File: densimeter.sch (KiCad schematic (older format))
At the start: 3 parts, among them IC1 XGZP6897A

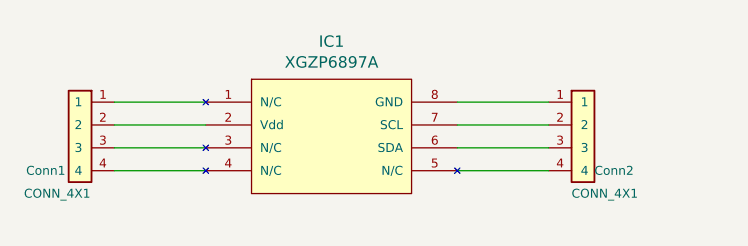
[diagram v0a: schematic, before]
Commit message: added 100 nF capacitor C1
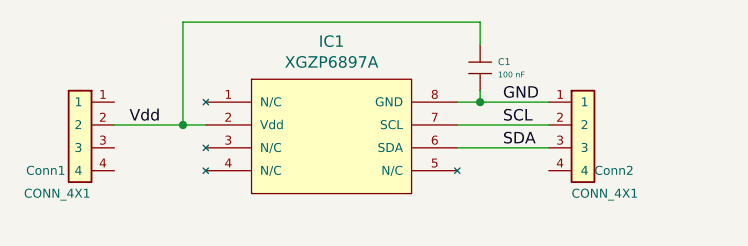
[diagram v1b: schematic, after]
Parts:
- added C1: 100 nF, Capacitor_SMD:C_0805_2012Metric, symbol thmalmeida:C_Micro
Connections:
- net at IC1.1 (N/C): no longer Conn1.1
- net Vdd: now reaches Conn1.2, IC1.2 (Vdd)
- net Vdd: now also C1.1 (A)
- net at IC1.3 (N/C): no longer Conn1.3
- net at IC1.4 (N/C): no longer Conn1.4
- net at IC1.5 (N/C): no longer Conn2.4
- net SDA: now reaches Conn2.3, IC1.6 (SDA)
- net SCL: now reaches Conn2.2, IC1.7 (SCL)
- net GND: now reaches Conn2.1, IC1.8 (GND)
- net GND: now also C1.2 (B)
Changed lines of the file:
@@
 $EndComp
 Wire Wire Line
-	4950 3300 4550 3300
+	4950 3300 4850 3300
 Wire Wire Line
-	4550 3400 4950 3400
-Wire Wire Line
-	4950 3500 4550 3500
-Wire Wire Line
-	4550 3200 4950 3200
-Wire Wire Line
-	6050 3200 6450 3200
+	6050 3200 6150 3200
 Wire Wire Line
 	6450 3300 6050 3300
@@
 	6050 3400 6450 3400
 Wire Wire Line
-	6450 3500 6050 3500
+	6150 3150 6150 3200
+Connection ~ 6150 3200
+Wire Wire Line
+	6150 3200 6450 3200
+Wire Wire Line
+	6150 2950 6150 2850
+Wire Wire Line
+	6150 2850 4850 2850
+Wire Wire Line
+	4850 2850 4850 3300
+Connection ~ 4850 3300
+Wire Wire Line
+	4850 3300 4550 3300
+$Comp
+L thmalmeida:C_Micro C1
+U 1 1 615E0BAC
+P 6150 3050
+F 0 "C1" H 6228 3076 30  0000 L CNN
+F 1 "100 nF" H 6228 3020 25  0000 L CNN
+F 2 "Capacitor_SMD:C_0805_2012Metric" H 6400 2700 60  0001 C CNN
+F 3 "" H 6190 3100 60  0000 C CNN
+F 4 "xx" H 6400 3200 60  0001 C CNN "Rated Voltage [V]"
+F 5 "xx" H 6400 3300 60  0001 C CNN "Tolerance [%]"
+F 6 "xxxx" H 6400 3100 60  0001 C CNN "Part Number"
+F 7 "yyyy" H 6400 3000 60  0001 C CNN "Manufacture"
+F 8 "xxx" H 6400 2900 60  0001 C CNN "Module"
+F 9 "yes" H 6400 2800 60  0001 C CNN "Placed Onboard?"
+	1    6150 3050
+	1    0    0    -1
+$EndComp
+Text Label 6250 3200 0    50   ~ 0
+GND
+Text Label 6250 3300 0    50   ~ 0
+SCL
+Text Label 6250 3400 0    50   ~ 0
+SDA
+Text Label 4750 3300 2    50   ~ 0
+Vdd
 $EndSCHEMATC

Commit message: 4 pins module
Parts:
- removed Conn1: CONN_4X1, Connector_PinHeader_2.54mm:PinHeader_1x04_P2.54mm_Vertical, symbol thmalmeida:CONN_4X1
- renumbered Conn2 to Conn1
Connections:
- net SCL: now also Conn1.1; no longer Conn1.2
- net SDA: now also Conn1.2; no longer Conn1.3
- net Vdd: now also Conn1.3
- net Gnd: now reaches Conn1.4
- net Gnd: now also C1.2 (B), IC1.8 (GND)
- removed net GND: C1.2 (B), Conn1.1, IC1.8 (GND)
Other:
- moved on the sheet: Conn1
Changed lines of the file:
@@
 $Comp
 L thmalmeida:CONN_4X1 Conn1
-U 1 1 615DF409
-P 4400 3350
-F 0 "Conn1" H 4550 3200 39  0000 C CNN
-F 1 "CONN_4X1" H 4500 3100 39  0000 C CNN
-F 2 "Connector_PinHeader_2.54mm:PinHeader_1x04_P2.54mm_Vertical" H 4430 3080 60  0001 C CNN
-F 3 "" H 4400 3600 60  0000 C CNN
-F 4 "xxxx" H 4400 3650 60  0001 C CNN "Part Number"
-F 5 "MM" H 4400 3750 60  0001 C CNN "Manufacturer"
-F 6 "mm" H 4400 3850 60  0001 C CNN "Module"
-F 7 "no" H 4400 3950 60  0001 C CNN "Placed Onboard?"
-	1    4400 3350
-	-1   0    0    -1
-$EndComp
-$Comp
-L thmalmeida:CONN_4X1 Conn2
 U 1 1 615DF971
-P 6600 3350
-F 0 "Conn2" H 6650 3200 39  0000 L CNN
-F 1 "CONN_4X1" H 6550 3100 39  0000 L CNN
-F 2 "Connector_PinHeader_2.54mm:PinHeader_1x04_P2.54mm_Vertical" H 6630 3080 60  0001 C CNN
-F 3 "" H 6600 3600 60  0000 C CNN
-F 4 "xxxx" H 6600 3650 60  0001 C CNN "Part Number"
-F 5 "MM" H 6600 3750 60  0001 C CNN "Manufacturer"
-F 6 "mm" H 6600 3850 60  0001 C CNN "Module"
-F 7 "no" H 6600 3950 60  0001 C CNN "Placed Onboard?"
-	1    6600 3350
+P 6600 3450
+F 0 "Conn1" V 6700 3300 39  0000 L CNN
+F 1 "CONN_4X1" H 6450 3200 39  0000 L CNN
+F 2 "Connector_PinHeader_2.54mm:PinHeader_1x04_P2.54mm_Vertical" H 6630 3180 60  0001 C CNN
+F 3 "" H 6600 3700 60  0000 C CNN
+F 4 "xxxx" H 6600 3750 60  0001 C CNN "Part Number"
+F 5 "MM" H 6600 3850 60  0001 C CNN "Manufacturer"
+F 6 "mm" H 6600 3950 60  0001 C CNN "Module"
+F 7 "no" H 6600 4050 60  0001 C CNN "Placed Onboard?"
+	1    6600 3450
 	1    0    0    -1
 $EndComp
@@
 Connection ~ 6150 3200
 Wire Wire Line
-	6150 3200 6450 3200
-Wire Wire Line
 	6150 2950 6150 2850
 Wire Wire Line
@@
 Wire Wire Line
 	4850 2850 4850 3300
-Connection ~ 4850 3300
-Wire Wire Line
-	4850 3300 4550 3300
 $Comp
 L thmalmeida:C_Micro C1
@@
 	1    0    0    -1
 $EndComp
-Text Label 6250 3200 0    50   ~ 0
-GND
+Text Label 6400 3600 2    50   ~ 0
+Gnd
 Text Label 6250 3300 0    50   ~ 0
 SCL
 Text Label 6250 3400 0    50   ~ 0
 SDA
-Text Label 4750 3300 2    50   ~ 0
+Text Label 6400 3500 2    50   ~ 0
 Vdd
+Wire Wire Line
+	4850 3300 4850 3700
+Wire Wire Line
+	4850 3700 6150 3700
+Wire Wire Line
+	6150 3700 6150 3500
+Wire Wire Line
+	6150 3500 6450 3500
+Connection ~ 4850 3300
+Wire Wire Line
+	6750 3200 6750 3750
+Wire Wire Line
+	6750 3750 6400 3750
+Wire Wire Line
+	6400 3750 6400 3600
+Wire Wire Line
+	6400 3600 6450 3600
+Wire Wire Line
+	6150 3200 6750 3200
 $EndSCHEMATC

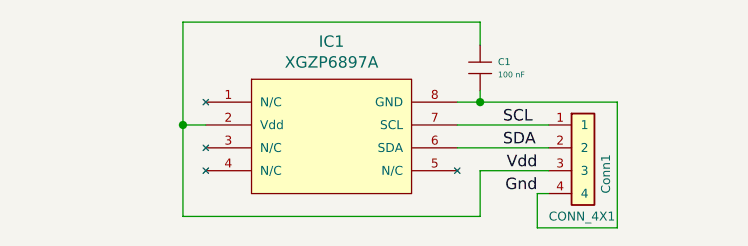
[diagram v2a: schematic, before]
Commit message: pull up resistors added
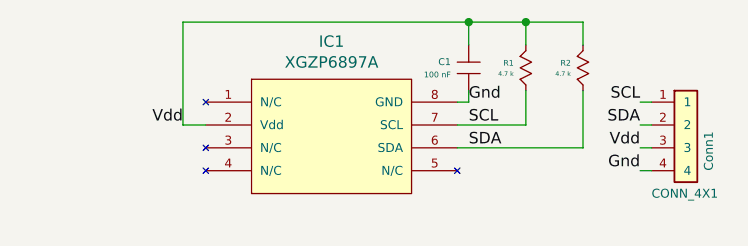
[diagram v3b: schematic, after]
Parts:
- added R1, R2: 4.7 k, Resistor_SMD:R_0805_2012Metric, symbol thmalmeida:R_Micro
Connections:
- net SCL: now also R1.1 (A)
- net SDA: now also R2.1 (A)
- net Vdd: now also R1.2 (B), R2.2 (B)
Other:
- moved on the sheet: C1, Conn1
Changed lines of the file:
@@
 L thmalmeida:CONN_4X1 Conn1
 U 1 1 615DF971
-P 6600 3450
-F 0 "Conn1" V 6700 3300 39  0000 L CNN
-F 1 "CONN_4X1" H 6450 3200 39  0000 L CNN
-F 2 "Connector_PinHeader_2.54mm:PinHeader_1x04_P2.54mm_Vertical" H 6630 3180 60  0001 C CNN
-F 3 "" H 6600 3700 60  0000 C CNN
-F 4 "xxxx" H 6600 3750 60  0001 C CNN "Part Number"
-F 5 "MM" H 6600 3850 60  0001 C CNN "Manufacturer"
-F 6 "mm" H 6600 3950 60  0001 C CNN "Module"
-F 7 "no" H 6600 4050 60  0001 C CNN "Placed Onboard?"
-	1    6600 3450
+P 7050 3350
+F 0 "Conn1" V 7150 3200 39  0000 L CNN
+F 1 "CONN_4X1" H 6900 3100 39  0000 L CNN
+F 2 "Connector_PinHeader_2.54mm:PinHeader_1x04_P2.54mm_Vertical" H 7080 3080 60  0001 C CNN
+F 3 "" H 7050 3600 60  0000 C CNN
+F 4 "xxxx" H 7050 3650 60  0001 C CNN "Part Number"
+F 5 "MM" H 7050 3750 60  0001 C CNN "Manufacturer"
+F 6 "mm" H 7050 3850 60  0001 C CNN "Module"
+F 7 "no" H 7050 3950 60  0001 C CNN "Placed Onboard?"
+	1    7050 3350
 	1    0    0    -1
 $EndComp
@@
 	4950 3300 4850 3300
 Wire Wire Line
-	6050 3200 6150 3200
+	6050 3200 6100 3200
 Wire Wire Line
-	6450 3300 6050 3300
-Wire Wire Line
-	6050 3400 6450 3400
-Wire Wire Line
-	6150 3150 6150 3200
-Connection ~ 6150 3200
-Wire Wire Line
-	6150 2950 6150 2850
-Wire Wire Line
-	6150 2850 4850 2850
+	6100 2850 4850 2850
 Wire Wire Line
 	4850 2850 4850 3300
+Text Label 6850 3200 2    50   ~ 0
+SCL
+Text Label 6850 3300 2    50   ~ 0
+SDA
+$Comp
+L thmalmeida:R_Micro R2
+U 1 1 615EBE8B
+P 6600 3050
+F 0 "R2" H 6547 3029 25  0000 R CNN
+F 1 "4.7 k" H 6547 3076 20  0000 R CNN
+F 2 "Resistor_SMD:R_0805_2012Metric" H 6675 2925 60  0001 C CNN
+F 3 "" V 6650 3120 60  0000 C CNN
+F 4 "0.1" H 6600 3625 60  0001 C CNN "Rated Power [W]"
+F 5 "5" H 6600 3700 60  0001 C CNN "Tolerance [%]"
+F 6 "MCT08050F1001C" H 6600 3300 60  0001 C CNN "Part Number"
+F 7 "VISHAY" H 6600 3400 60  0001 C CNN "Manufacturer"
+F 8 "xx" H 6600 3500 60  0001 C CNN "Module"
+F 9 "yes" H 6600 3575 60  0001 C CNN "Placed Onboard?"
+	1    6600 3050
+	1    0    0    1
+$EndComp
+Text Label 6100 3300 0    50   ~ 0
+SCL
+Text Label 6100 3200 0    50   ~ 0
+Gnd
+Text Label 4850 3300 2    50   ~ 0
+Vdd
+Wire Wire Line
+	6100 3150 6100 3200
+Wire Wire Line
+	6100 2950 6100 2850
 $Comp
 L thmalmeida:C_Micro C1
 U 1 1 615E0BAC
-P 6150 3050
-F 0 "C1" H 6228 3076 30  0000 L CNN
-F 1 "100 nF" H 6228 3020 25  0000 L CNN
-F 2 "Capacitor_SMD:C_0805_2012Metric" H 6400 2700 60  0001 C CNN
-F 3 "" H 6190 3100 60  0000 C CNN
-F 4 "xx" H 6400 3200 60  0001 C CNN "Rated Voltage [V]"
-F 5 "xx" H 6400 3300 60  0001 C CNN "Tolerance [%]"
-F 6 "xxxx" H 6400 3100 60  0001 C CNN "Part Number"
-F 7 "yyyy" H 6400 3000 60  0001 C CNN "Manufacture"
-F 8 "xxx" H 6400 2900 60  0001 C CNN "Module"
-F 9 "yes" H 6400 2800 60  0001 C CNN "Placed Onboard?"
-	1    6150 3050
-	1    0    0    -1
+P 6100 3050
+F 0 "C1" H 6178 3076 30  0000 L CNN
+F 1 "100 nF" H 6178 3020 25  0000 L CNN
+F 2 "Capacitor_SMD:C_0805_2012Metric" H 6350 2700 60  0001 C CNN
+F 3 "" H 6140 3100 60  0000 C CNN
+F 4 "xx" H 6350 3200 60  0001 C CNN "Rated Voltage [V]"
+F 5 "xx" H 6350 3300 60  0001 C CNN "Tolerance [%]"
+F 6 "xxxx" H 6350 3100 60  0001 C CNN "Part Number"
+F 7 "yyyy" H 6350 3000 60  0001 C CNN "Manufacture"
+F 8 "xxx" H 6350 2900 60  0001 C CNN "Module"
+F 9 "yes" H 6350 2800 60  0001 C CNN "Placed Onboard?"
+	1    6100 3050
+	-1   0    0    -1
 $EndComp
-Text Label 6400 3600 2    50   ~ 0
+Wire Wire Line
+	6100 2850 6350 2850
+Connection ~ 6100 2850
+$Comp
+L thmalmeida:R_Micro R1
+U 1 1 615F7F45
+P 6350 3050
+F 0 "R1" H 6297 3029 25  0000 R CNN
+F 1 "4.7 k" H 6297 3076 20  0000 R CNN
+F 2 "Resistor_SMD:R_0805_2012Metric" H 6425 2925 60  0001 C CNN
+F 3 "" V 6400 3120 60  0000 C CNN
+F 4 "0.1" H 6350 3625 60  0001 C CNN "Rated Power [W]"
+F 5 "5" H 6350 3700 60  0001 C CNN "Tolerance [%]"
+F 6 "MCT08050F1001C" H 6350 3300 60  0001 C CNN "Part Number"
+F 7 "VISHAY" H 6350 3400 60  0001 C CNN "Manufacturer"
+F 8 "xx" H 6350 3500 60  0001 C CNN "Module"
+F 9 "yes" H 6350 3575 60  0001 C CNN "Placed Onboard?"
+	1    6350 3050
+	1    0    0    1
+$EndComp
+Text Label 6100 3400 0    50   ~ 0
+SDA
+Wire Wire Line
+	6350 3300 6350 3150
+Wire Wire Line
+	6050 3300 6350 3300
+Wire Wire Line
+	6350 2950 6350 2850
+Connection ~ 6350 2850
+Wire Wire Line
+	6600 3400 6600 3150
+Wire Wire Line
+	6050 3400 6600 3400
+Wire Wire Line
+	6600 2850 6600 2950
+Wire Wire Line
+	6350 2850 6600 2850
+Wire Wire Line
+	6850 3300 6900 3300
+Wire Wire Line
+	6850 3200 6900 3200
+Wire Wire Line
+	6850 3500 6900 3500
+Text Label 6850 3500 2    50   ~ 0
 Gnd
-Text Label 6250 3300 0    50   ~ 0
-SCL
-Text Label 6250 3400 0    50   ~ 0
-SDA
-Text Label 6400 3500 2    50   ~ 0
+Text Label 6850 3400 2    50   ~ 0
 Vdd
 Wire Wire Line
-	4850 3300 4850 3700
-Wire Wire Line
-	4850 3700 6150 3700
-Wire Wire Line
-	6150 3700 6150 3500
-Wire Wire Line
-	6150 3500 6450 3500
-Connection ~ 4850 3300
-Wire Wire Line
-	6750 3200 6750 3750
-Wire Wire Line
-	6750 3750 6400 3750
-Wire Wire Line
-	6400 3750 6400 3600
-Wire Wire Line
-	6400 3600 6450 3600
-Wire Wire Line
-	6150 3200 6750 3200
+	6900 3400 6850 3400
 $EndSCHEMATC
